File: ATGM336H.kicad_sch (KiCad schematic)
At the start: 8 parts, among them IC1 ATGM336H-5N31, U9 M24C32

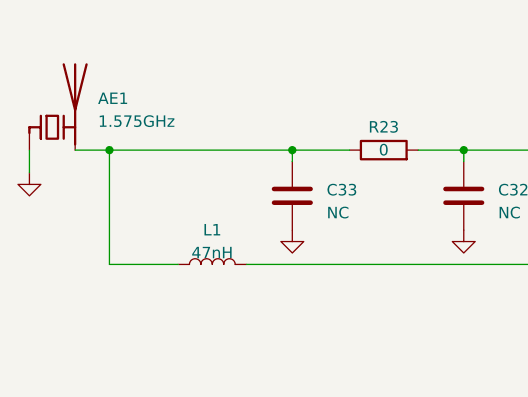
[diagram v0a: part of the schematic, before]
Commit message: assigned footprints and checked the schematic
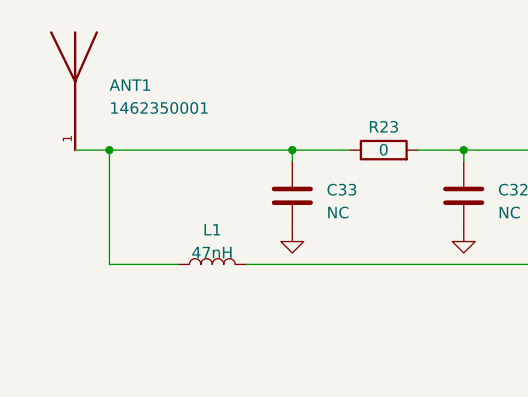
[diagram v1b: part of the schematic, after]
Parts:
- removed AE1: 1.575GHz, symbol Device:Antenna_Chip
- added ANT1: 1462350001, Molex GPS antenna:ANT_1462350001, symbol 1462350001:1462350001
- C15, C32, C33: footprint (none) -> Capacitor_SMD:C_0402_1005Metric_Pad0.74x0.62mm_HandSolder
- L1: footprint (none) -> Inductor_SMD:L_0402_1005Metric
- R23: footprint (none) -> Resistor_SMD:R_0402_1005Metric_Pad0.72x0.64mm_HandSolder
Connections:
- net at C33.1, L1.1, R23.1: now also ANT1.1
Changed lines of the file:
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@@
   (no_connect (at 137.16 91.44))
   (no_connect (at 137.16 99.06))
-  (wire (pts (xy 68.58 83.82) (xy 68.58 81.28))
-    (stroke (width 0) (type default))
-  )
   (wire (pts (xy 147.32 130.81) (xy 147.32 133.35))
     (stroke (width 0) (type default))
@@
     )
   )
+  (symbol (lib_id "1462350001:1462350001") (at 73.66 76.2 0) (unit 1)
+    (in_bom yes) (on_board yes) (dnp no) (fields_autoplaced)
+    (property "Reference" "ANT1" (at 77.47 74.1045 0)
+      (effects (font (size 1.27 1.27)) (justify left))
+    )
+    (property "Value" "1462350001" (at 77.47 76.6445 0)
+      (effects (font (size 1.27 1.27)) (justify left))
+    )
+    (property "Footprint" "Molex GPS antenna:ANT_1462350001" (at 73.66 76.2 0)
+      (effects (font (size 1.27 1.27)) (justify bottom) hide)
+    )
+    (property "Datasheet" "" (at 73.66 76.2 0)
+      (effects (font (size 1.27 1.27)) hide)
+    )
+    (property "PARTREV" "B" (at 73.66 76.2 0)
+      (effects (font (size 1.27 1.27)) (justify bottom) hide)
+    )
+    (property "MANUFACTURER" "Molex" (at 73.66 76.2 0)
+      (effects (font (size 1.27 1.27)) (justify bottom) hide)
+    )
+    (property "STANDARD" "Manufacturer Recommendation" (at 73.66 76.2 0)
+      (effects (font (size 1.27 1.27)) (justify bottom) hide)
+    )
+    (pin "1")
+    (instances
+      (project "RP2040_SOS_band"
+        (path "/1d911b84-17e1-4d47-ac8f-a730104b53ed/2e6f74bb-681c-49d2-acf8-32965dc28494"
+          (reference "ANT1") (unit 1)
+        )
+      )
+    )
+  )
   (symbol (lib_id "power:GND") (at 175.26 99.06 0) (unit 1)
     (in_bom yes) (on_board yes) (dnp no) (fields_autoplaced)
@@
       (effects (font (size 1.27 1.27)) (justify left))
     )
-    (property "Footprint" "" (at 117.8052 90.17 0)
+    (property "Footprint" "Capacitor_SMD:C_0402_1005Metric_Pad0.74x0.62mm_HandSolder" (at 117.8052 90.17 0)
       (effects (font (size 1.27 1.27)) hide)
     )
@@
       (effects (font (size 1.27 1.27)))
     )
-    (property "Footprint" "" (at 88.9 93.98 0)
+    (property "Footprint" "Inductor_SMD:L_0402_1005Metric" (at 88.9 93.98 0)
       (effects (font (size 1.27 1.27)) hide)
     )
@@
       (effects (font (size 1.27 1.27)) (justify left))
     )
-    (property "Footprint" "" (at 190.1952 91.44 0)
+    (property "Footprint" "Capacitor_SMD:C_0402_1005Metric_Pad0.74x0.62mm_HandSolder" (at 190.1952 91.44 0)
       (effects (font (size 1.27 1.27)) hide)
     )
@@
       (effects (font (size 1.27 1.27)) (justify left))
     )
-    (property "Footprint" "" (at 98.7552 90.17 0)
+    (property "Footprint" "Capacitor_SMD:C_0402_1005Metric_Pad0.74x0.62mm_HandSolder" (at 98.7552 90.17 0)
       (effects (font (size 1.27 1.27)) hide)
     )
@@
       (effects (font (size 1.27 1.27)))
     )
-    (property "Footprint" "" (at 107.95 83.058 90)
+    (property "Footprint" "Resistor_SMD:R_0402_1005Metric_Pad0.72x0.64mm_HandSolder" (at 107.95 83.058 90)
       (effects (font (size 1.27 1.27)) hide)
     )
@@
         (path "/1d911b84-17e1-4d47-ac8f-a730104b53ed/2e6f74bb-681c-49d2-acf8-32965dc28494"
           (reference "R24") (unit 1)
-        )
-      )
-    )
-  )
-  (symbol (lib_id "power:GND") (at 68.58 83.82 0) (unit 1)
-    (in_bom yes) (on_board yes) (dnp no) (fields_autoplaced)
-    (property "Reference" "#PWR051" (at 68.58 90.17 0)
-      (effects (font (size 1.27 1.27)) hide)
-    )
-    (property "Value" "GND" (at 68.58 88.9 0) (do_not_autoplace)
-      (effects (font (size 1.27 1.27)) hide)
-    )
-    (property "Footprint" "" (at 68.58 83.82 0)
-      (effects (font (size 1.27 1.27)) hide)
-    )
-    (property "Datasheet" "" (at 68.58 83.82 0)
-      (effects (font (size 1.27 1.27)) hide)
-    )
-    (pin "1")
-    (instances
-      (project "RP2040_SOS_band"
-        (path "/1d911b84-17e1-4d47-ac8f-a730104b53ed/2e6f74bb-681c-49d2-acf8-32965dc28494"
-          (reference "#PWR051") (unit 1)
         )
       )
@@
         )
       )
-    )
-  )
-  (symbol (lib_id "Device:Antenna_Chip") (at 71.12 78.74 0) (unit 1)
-    (in_bom yes) (on_board yes) (dnp no) (fields_autoplaced)
-    (property "Reference" "AE1" (at 76.2 75.565 0)
-      (effects (font (size 1.27 1.27)) (justify left))
-    )
-    (property "Value" "1.575GHz" (at 76.2 78.105 0)
-      (effects (font (size 1.27 1.27)) (justify left))
-    )
-    (property "Footprint" "" (at 68.58 74.295 0)
-      (effects (font (size 1.27 1.27)) hide)
-    )
-    (property "Datasheet" "~" (at 68.58 74.295 0)
-      (effects (font (size 1.27 1.27)) hide)
-    )
-    (pin "1")
-    (pin "2")
-    (instances
-      (project "RP2040_SOS_band"
-        (path "/1d911b84-17e1-4d47-ac8f-a730104b53ed/2e6f74bb-681c-49d2-acf8-32965dc28494"
-          (reference "AE1") (unit 1)
-        )
-      )

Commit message: bottom board conn. done
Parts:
- removed ANT1: 1462350001, Molex GPS antenna:ANT_1462350001, symbol 1462350001:1462350001
- removed C32, C33: NC, Capacitor_SMD:C_0402_1005Metric_Pad0.74x0.62mm_HandSolder, symbol Device:C
- removed IC1: ATGM336H-5N31, ATGM336H-5N31:ATGM336H5N31, symbol ATGM336H-5N31:ATGM336H-5N31
- removed L1: 47nH, Inductor_SMD:L_0402_1005Metric, symbol Device:L
- removed R23: 0, Resistor_SMD:R_0402_1005Metric_Pad0.72x0.64mm_HandSolder, symbol Device:R
- removed U9: M24C32, Package_SO:TSSOP-8_4.4x3mm_P0.65mm, symbol Memory_EEPROM:24LC32
- added C10: 0.1uF, Capacitor_SMD:C_0402_1005Metric_Pad0.74x0.62mm_HandSolder, symbol Device:C
- added C11: 10pF, Capacitor_SMD:C_0402_1005Metric_Pad0.74x0.62mm_HandSolder, symbol Device:C
- added U8: L96, L96 (1):XCVR_L96, symbol L96:L96
- C15: value 10uF -> 100pF
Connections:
- net GND: now also C10.2, C11.2, U8.10 (GND), U8.11 (GND), U8.12 (GND), U8.13 (GND), U8.14 (GND), U8.15 (GND), U8.18 (GND), U8.19 (GND), U8.21 (GND), U8.22 (GND), U8.27 (GND), U8.31 (GND), U8.4 (GND), U8.5 (GND)
- net VDD_3.3 renamed VDD_3.3_t
- net VDD_3.3_t: now also C10.1, C11.1, U8.8 (V_BCKP), U8.9 (VCC)
- new net: U8.16 (RF_OUT), U8.17 (RF_IN)
- new net Force_ON_t: U8.28 (FORCE_ON)
- new net GPS_RXD_t: U8.26 (RXD1)
- new net GPS_TXD_t: U8.25 (TXD1)
- no-connect marks 4 -> 9
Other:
- moved on the sheet: C15
